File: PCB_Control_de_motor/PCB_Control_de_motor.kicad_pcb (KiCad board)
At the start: 2 copper layers, 100 x 50 mm, 0 parts

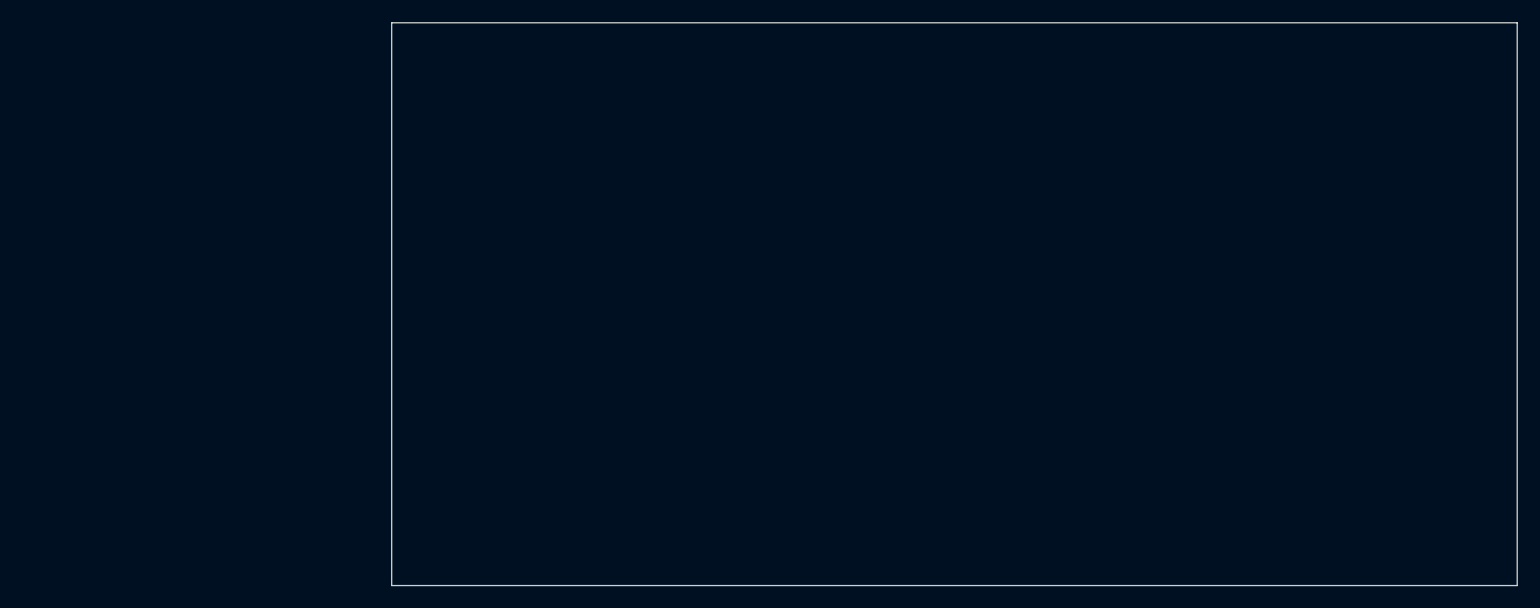
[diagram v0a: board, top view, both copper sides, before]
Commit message: Agregado de diodos TVS y avance del PCB con fuente y micro listo
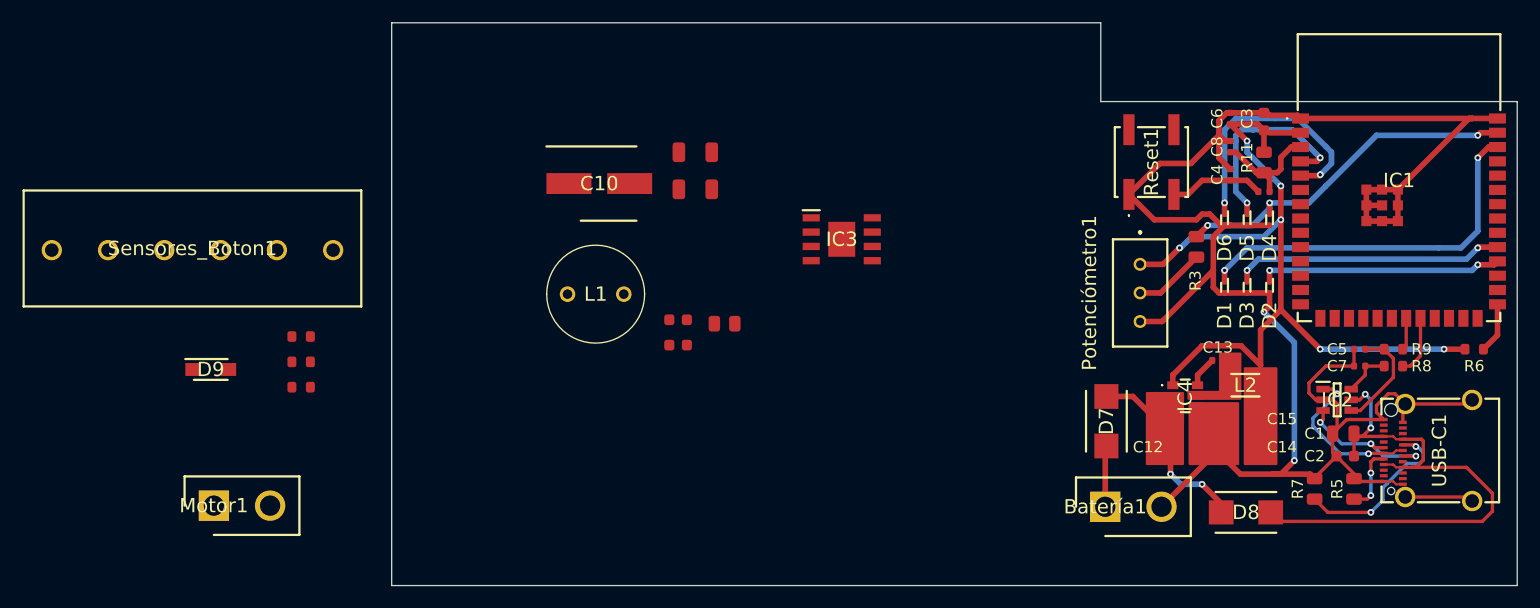
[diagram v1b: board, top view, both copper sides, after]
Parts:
- added Batería1: XT30UPB-M, SamacSys_Parts:SHDR2W160P0X500_1X2_1020X520X1070P, F.Cu at (153.4, 113.0)
- added C1: 22uF, PCM_JLCPCB:C_0805, F.Cu at (174.6, 106.5)
- added C10: 47uF, SamacSys_Parts:CAPAE660X820N, F.Cu at (108.4, 84.3)
- added C11: 100nF, PCM_JLCPCB:C_0603, F.Cu at (115.4, 98.6)
- added C12: 10uF, PCM_JLCPCB:C_0805, F.Cu at (160.7, 107.7)
- added C13: 100nF, PCM_JLCPCB:C_0402, F.Cu at (163.4, 100.0)
- added C14: 22uF, PCM_JLCPCB:C_0805, F.Cu at (165.6, 107.7)
- added C15: 22uF, PCM_JLCPCB:C_0805, F.Cu at (165.6, 105.2)
- added C2: 100nF, PCM_JLCPCB:C_0603, F.Cu at (174.7, 108.5)
- added C3: 22uF, PCM_JLCPCB:C_0603, F.Cu at (167.5, 78.8)
- added C4: 100nF, PCM_JLCPCB:C_0402, F.Cu at (164.5, 83.5)
- added C5: 1uF, PCM_JLCPCB:C_0402, F.Cu at (176.0, 99.0)
- added C6: 100nF, PCM_JLCPCB:C_0402, F.Cu at (164.5, 78.5)
- added C7: 1uF, PCM_JLCPCB:C_0402, F.Cu at (176.0, 100.5)
- added C8: 1uF, PCM_JLCPCB:C_0402, F.Cu at (164.5, 81.0)
- added C9: 100nF, PCM_JLCPCB:C_0603, F.Cu at (115.4, 96.4)
- added D1: ESD9B3.3ST5G, SamacSys_Parts:SODFL1006X40N, F.Cu at (164.0, 93.5)
- added D2: ESD9B3.3ST5G, SamacSys_Parts:SODFL1006X40N, F.Cu at (168.0, 93.5)
- added D3: ESD9B3.3ST5G, SamacSys_Parts:SODFL1006X40N, F.Cu at (166.0, 93.5)
- added D4: ESD9B3.3ST5G, SamacSys_Parts:SODFL1006X40N, F.Cu at (168.0, 87.5)
- added D5: ESD9B3.3ST5G, SamacSys_Parts:SODFL1006X40N, F.Cu at (166.0, 87.5)
- added D6: ESD9B3.3ST5G, SamacSys_Parts:SODFL1006X40N, F.Cu at (164.0, 87.5)
- added D7: SS210-E3_52T, SamacSys_Parts:DIONM5436X244N, F.Cu at (153.5, 105.4)
- added D8: SS210-E3_52T, SamacSys_Parts:DIONM5436X244N, F.Cu at (165.9, 113.5)
- added D9: SMF3.3, SamacSys_Parts:SOD3718X108N, F.Cu at (73.9, 100.8)
- added IC1: ESP32-S3-WROOM-1-N16, SamacSys_Parts:ESP32S3WROOM1N16, F.Cu at (179.5, 83.8)
- added IC2: USBLC6-2SC6, SamacSys_Parts:SOT95P280X145-6N, F.Cu at (174.0, 103.5)
- added IC3: DRV8871DDAR, SamacSys_Parts:SOIC127P600X170-9N, F.Cu at (130.0, 89.2)
- added IC4: AP63203WU-7, SamacSys_Parts:AP63203WU7, F.Cu at (160.5, 103.2)
- added L1: 100mH, SamacSys_Parts:RLB1014104KL, F.Cu at (105.6, 94.1)
- added L2: NLV25T-3R9J-PF, SamacSys_Parts:INDM2520X190N, F.Cu at (165.8, 102.2)
- added Motor1: XT30UPB-M, SamacSys_Parts:SHDR2W160P0X500_1X2_1020X520X1070P, F.Cu at (74.2, 112.9)
- added Potenciómetro1: 20k, SamacSys_Parts:3296W1503LF, F.Cu at (156.5, 91.5)
- added R1: 10kΩ, PCM_JLCPCB:R_0603, F.Cu at (82.0, 97.9)
- added R10: 0Ω, PCM_JLCPCB:R_0402, F.Cu at (167.5, 85.0)
- added R11: 10kΩ, PCM_JLCPCB:R_0805, F.Cu at (167.5, 82.4)
- added R12: 4.7kΩ, PCM_JLCPCB:R_1206, F.Cu at (117.0, 81.5)
- added R13: 4.7kΩ, PCM_JLCPCB:R_1206, F.Cu at (117.0, 84.8)
- added R14: 30kΩ, PCM_JLCPCB:R_0805, F.Cu at (119.6, 96.7)
- added R2: 10kΩ, PCM_JLCPCB:R_0603, F.Cu at (82.0, 100.1)
- added R3: 1kΩ, PCM_JLCPCB:R_0805, F.Cu at (161.5, 89.9)
- added R4: 10kΩ, PCM_JLCPCB:R_0603, F.Cu at (82.0, 102.4)
- added R5: 5.1kΩ, PCM_JLCPCB:R_0805, F.Cu at (175.5, 111.4)
- added R6: 4.7kΩ, PCM_JLCPCB:R_0603, F.Cu at (186.2, 99.0)
- added R7: 5.1kΩ, PCM_JLCPCB:R_0805, F.Cu at (172.0, 111.4)
- added R8: 33Ω, PCM_JLCPCB:R_0603, F.Cu at (179.0, 100.5)
- added R9: 33Ω, PCM_JLCPCB:R_0603, F.Cu at (179.0, 99.0)
- added Reset1: B3SL-1022P, SamacSys_Parts:B3SL1022P, F.Cu at (157.5, 82.4)
- added Sensores_Boton1: WJ128V-5.0-6P, SamacSys_Parts:WJ128V506P, F.Cu at (59.8, 90.2)
- added USB-C1: 12401832E402A, SamacSys_Parts:12401832E402A, F.Cu at (183.2, 108.0)
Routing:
- net GND: track 0.00 -> 181.5 mm, vias 0 -> 2
- net +3.3V: track 0.00 -> 75.5 mm, vias 0 -> 6
- net /5v_USB: track 0.00 -> 50.1 mm, vias 0 -> 2
- net /BOTON: track 0.00 -> 33.6 mm, vias 0 -> 2
- net /ADC: track 0.00 -> 31.9 mm, vias 0 -> 3
- net /LSC: track 0.00 -> 24.1 mm, vias 0 -> 2
- net /Driver/IN_2: track 0.00 -> 22.9 mm, vias 0 -> 2
- net /LSA: track 0.00 -> 21.6 mm, vias 0 -> 2
- net Net-(D7-K): track 0.00 -> 19.6 mm, vias 0 -> 2
- net /Driver/IN_1: track 0.00 -> 18.0 mm, vias 0 -> 2
- net Net-(USB-C1-CC2): track 0.00 -> 15.5 mm, vias 0 -> 2
- net Net-(IC2-I/O1_1): track 0.00 -> 14.4 mm, vias 0 -> 2
- net Net-(IC2-I/O2_1): track 0.00 -> 13.3 mm, vias 0 -> 3
- net EN_ESP32: track 0.00 -> 10.4 mm
- net Net-(IC2-I/O2_2): track 0.00 -> 9.49 mm
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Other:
- outline, holes or cut-outs redrawn

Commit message: PCB casi terminado
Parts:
- moved D9 95.7 mm to (169.6, 102.1), turned to -90 degrees
- moved Sensores_Boton1 90.0 mm to (148.8, 76.8), turned to 180 degrees
- moved R4 68.2 mm to (149.8, 95.8), turned to 90 degrees
- moved R1 68.0 mm to (149.8, 92.7), turned to 90 degrees
- moved R2 67.9 mm to (149.8, 99.0), turned to 90 degrees
- moved Motor1 50.7 mm to (123.2, 99.8), turned to -90 degrees
- moved L1 34.5 mm to (137.1, 108.3), turned to -90 degrees
- moved C11 30.0 mm to (143.0, 110.5), turned to 90 degrees
- moved R12 29.3 mm to (145.1, 89.7), turned to 90 degrees
- moved R13 25.5 mm to (142.0, 89.7), turned to 90 degrees
- moved C10 25.1 mm to (132.7, 90.7), turned to 180 degrees
- moved C9 22.4 mm to (137.8, 96.9)
- moved R14 21.6 mm to (141.2, 96.9), turned to 180 degrees
- moved IC3 15.2 mm to (139.6, 101.0), turned to 180 degrees
- moved C12 1.20 mm to (159.5, 108.0)
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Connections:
- C10 pad 2: GND -> Net-(C10--)
- C11 pad 2: Net-(IC3-PGND) -> Net-(C10--)
- IC3 pad 7: Net-(IC3-PGND) -> Net-(C10--)
- L1 pad 1: Net-(IC3-PGND) -> Net-(C10--)
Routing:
- net GND: track 181.5 -> 296.5 mm, vias 2 -> 4
- net /LSA: track 21.6 -> 100.9 mm, vias 2 -> 3
- net /LSC: track 24.1 -> 80.9 mm, vias 2 -> 3
- net /Driver/IN_2: track 22.9 -> 61.7 mm, vias 2 -> 4
- net /BOTON: track 33.6 -> 69.5 mm, vias 2 -> 3
- net /Driver/IN_1: track 18.0 -> 52.6 mm, vias 2 -> 4
- net +3.3V: track 75.5 -> 109.4 mm, vias 6 -> 10
- net Net-(C10--): track 0.00 -> 32.9 mm, vias 0 -> 3
- net +12V: track 5.44 -> 38.3 mm
- net Net-(D7-K): track 19.6 -> 24.4 mm
- net Net-(IC3-ILIM): track 0.00 -> 2.23 mm

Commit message: PCB listo
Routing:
- net Net-(C10--): vias 3 -> 22
- net GND: vias 4 -> 50
- added copper zone on B.Cu, net GND
- added copper zone on F.Cu, net GND
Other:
- board size 100 x 50 mm -> 71 x 47.5 mm

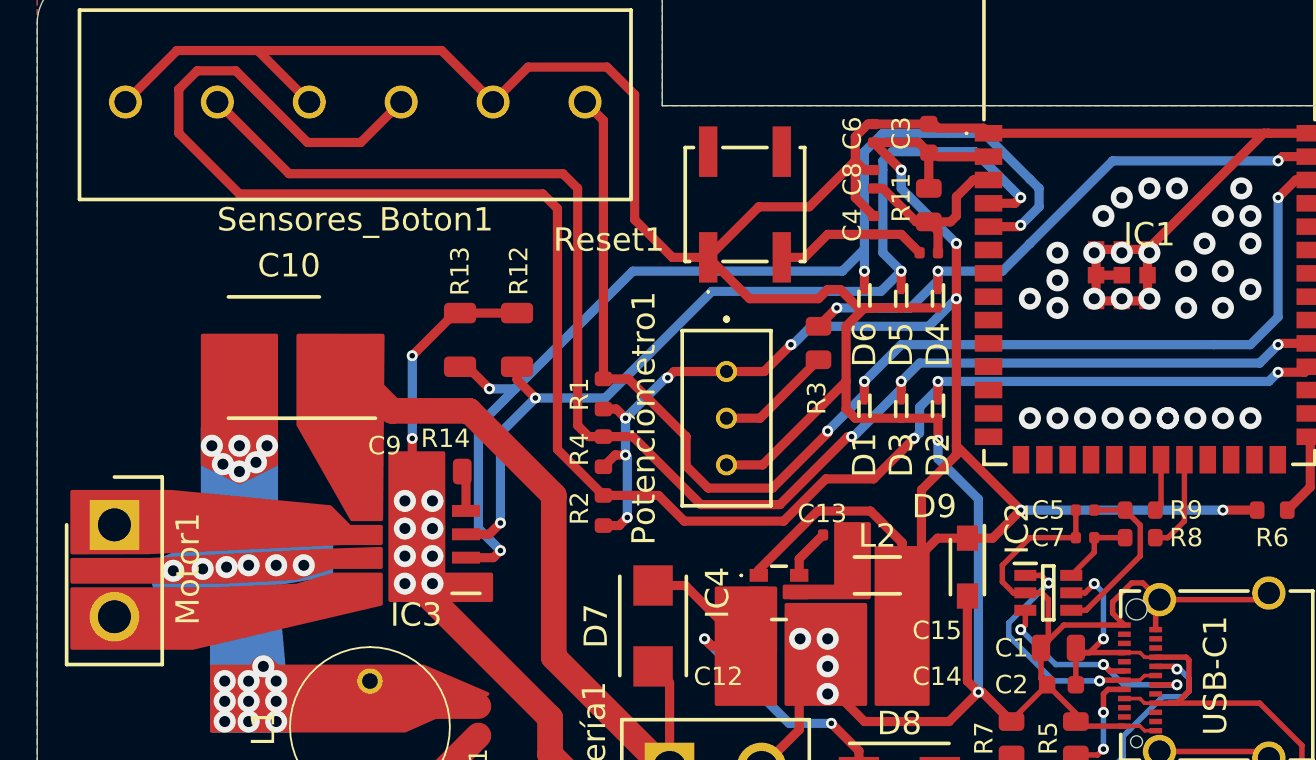
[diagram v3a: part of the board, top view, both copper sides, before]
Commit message: Correción del PCB, archivos de fabricación y BOM
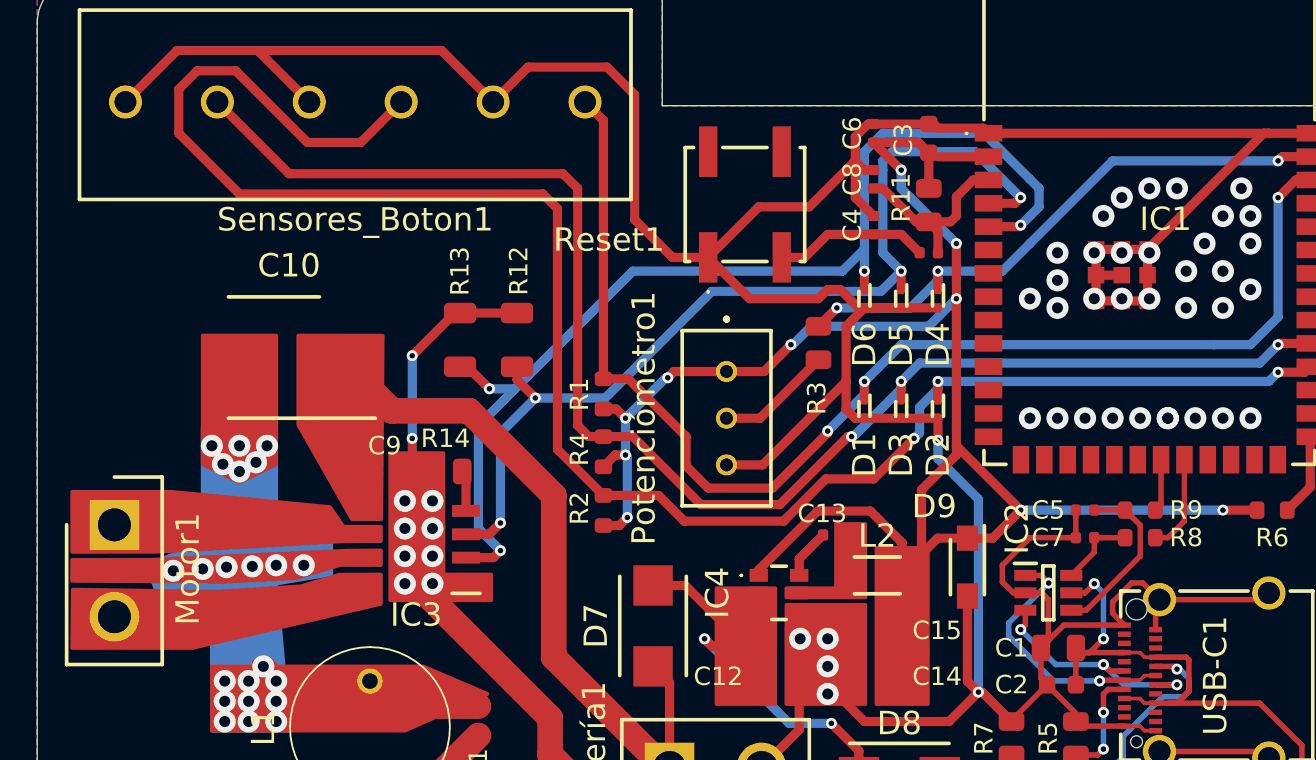
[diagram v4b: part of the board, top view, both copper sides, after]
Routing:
- net +3.3V: track 109.4 -> 108.3 mm
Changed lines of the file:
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@@
 	)
 	(setup
+		(stackup
+			(layer "F.SilkS"
+				(type "Top Silk Screen")
+			)
+			(layer "F.Paste"
+				(type "Top Solder Paste")
+			)
+			(layer "F.Mask"
+				(type "Top Solder Mask")
+				(thickness 0.01)
+			)
+			(layer "F.Cu"
+				(type "copper")
+				(thickness 0.035)
+			)
+			(layer "dielectric 1"
+				(type "core")
+				(thickness 1.51)
+				(material "FR4")
+				(epsilon_r 4.5)
+				(loss_tangent 0.02)
+			)
+			(layer "B.Cu"
+				(type "copper")
+				(thickness 0.035)
+			)
+			(layer "B.Mask"
+				(type "Bottom Solder Mask")
+				(thickness 0.01)
+			)
+			(layer "B.Paste"
+				(type "Bottom Solder Paste")
+			)
+			(layer "B.SilkS"
+				(type "Bottom Silk Screen")
+			)
+			(copper_finish "None")
+			(dielectric_constraints no)
+		)
 		(pad_to_mask_clearance 0)
 		(allow_soldermask_bridges_in_footprints no)
@@
 			(outputformat 1)
 			(mirror no)
-			(drillshape 1)
+			(drillshape 0)
 			(scaleselection 1)
-			(outputdirectory "")
+			(outputdirectory "Archivos_de_fabricacion/")
 		)
 	)
@@
 		(tags "Integrated Circuit")
 		(property "Reference" "IC1"
-			(at 0 0.25 0)
+			(at 0.88 -0.59 0)
 			(layer "F.SilkS")
 			(effects
@@
 		)
 		(fp_text user "${REFERENCE}"
-			(at 0 0.25 0)
+			(at 0.89 -0.58 0)
 			(layer "F.Fab")
 			(effects
@@
 		(tags "capacitor")
 		(property "Reference" "C3"
-			(at 0.28 -1.5 90)
+			(at -0.08 -1.38 90)
 			(layer "F.SilkS")
 			(effects
@@
 	(gr_poly
 		(pts
-			(xy 162.45 99.75) (xy 164.25 99.75) (xy 164.25 103.75) (xy 159.65 103.75) (xy 159.65 103.15) (xy 162.45 103.15)
+			(xy 162.45 99.75) (xy 164.05 99.75) (xy 164.05 103.75) (xy 159.75 103.75) (xy 159.75 103.25) (xy 162.45 103.25)
 		)
 		(stroke
@@
 	(gr_poly
 		(pts
-			(xy 137.7 101.1) (xy 134.7 101.2) (xy 125.158007 101.7) (xy 120.9 101.7) (xy 120.9 102.9) (xy 129.2 102.9)
-			(xy 133.1 102.7) (xy 135.1 102.1) (xy 137.7 102.1)
+			(xy 137.7 101.189281) (xy 135.92 101.2) (xy 125.158007 101.7) (xy 120.9 101.7) (xy 120.89 102.85)
+			(xy 129.2 102.9) (xy 133.1 102.7) (xy 135.466667 101.99) (xy 137.7 101.99)
 		)
 		(stroke
@@
 	(gr_poly
 		(pts
-			(xy 120.9 106.5) (xy 127.453844 106.5) (xy 137.7 104.1) (xy 137.7 102.5) (xy 135.149999 102.5) (xy 133.1 103.1)
-			(xy 128.50044 103.3) (xy 120.9 103.3)
+			(xy 120.9 106.5) (xy 127.453844 106.5) (xy 137.7 104.1) (xy 137.7 102.5) (xy 135.43 102.51) (xy 133.34 103.14)
+			(xy 128.73 103.44) (xy 120.93 103.32)
 		)
 		(stroke
@@
 	(gr_poly
 		(pts
-			(xy 120.9 98) (xy 126.3 98) (xy 134.932001 98.832001) (xy 136 99.9) (xy 137.7 99.9) (xy 137.7 100.8)
-			(xy 135.6 100.8) (xy 125 101.3) (xy 120.9 101.308614)
+			(xy 120.9 98) (xy 126.3 98) (xy 134.932001 98.832001) (xy 135.66 99.9) (xy 137.7 99.9) (xy 137.7 100.69)
+			(xy 135.61 100.7) (xy 125.564449 101.267963) (xy 120.9 101.277763)
 		)
 		(stroke
@@
 	)
 	(segment
-		(start 165.45 104.55)
-		(end 166.2 105.3)
-		(width 0.5)
-		(layer "F.Cu")
-		(net 3)
-	)
-	(segment
 		(start 170.975 100.525)
 		(end 172.5 99)
@@
 	)
 	(via
-		(at 130.5 102)
+		(at 132 109.4)
 		(size 1.2)
 		(drill 0.6)
@@
 	)
 	(via
-		(at 132 109.4)
+		(at 130 95.5)
 		(size 1.2)
 		(drill 0.6)
@@
 	)
 	(via
-		(at 130 95.5)
+		(at 130.7 102.06)
 		(size 1.2)
 		(drill 0.6)

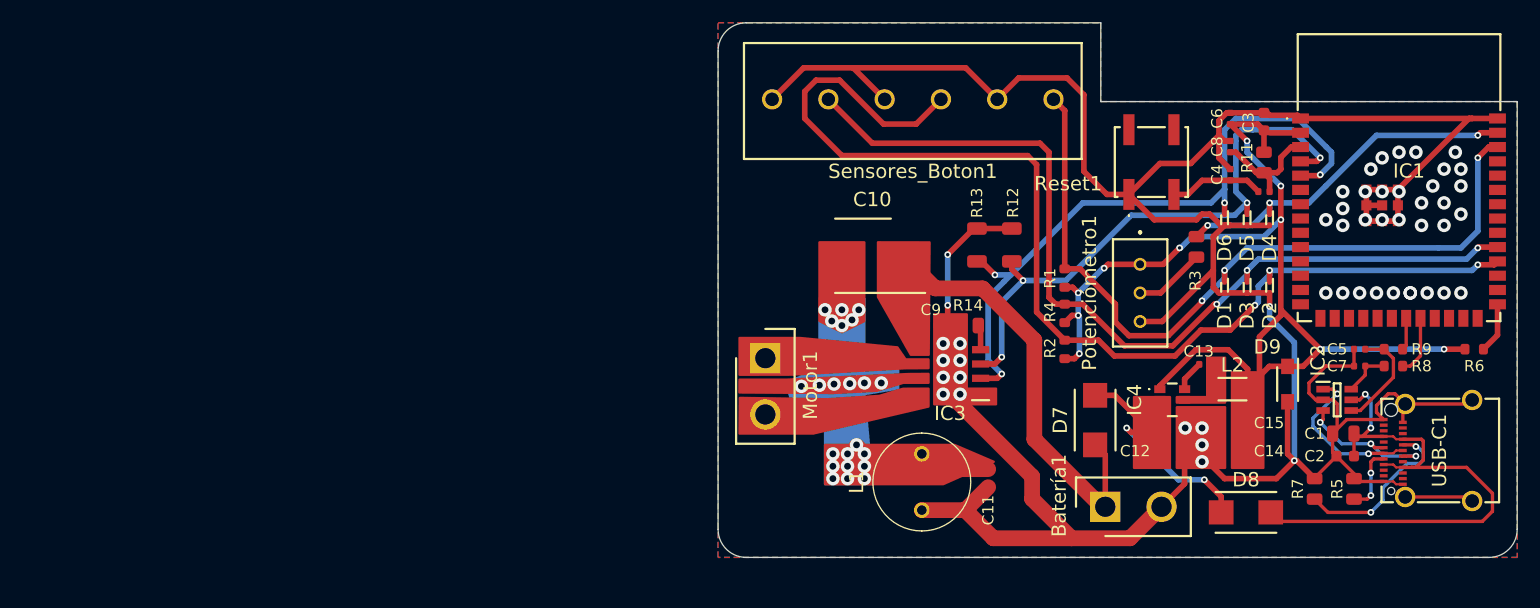
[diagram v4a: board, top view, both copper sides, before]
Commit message: Cambio del capacitor y rediseño de las pistas del driver con sus componentes
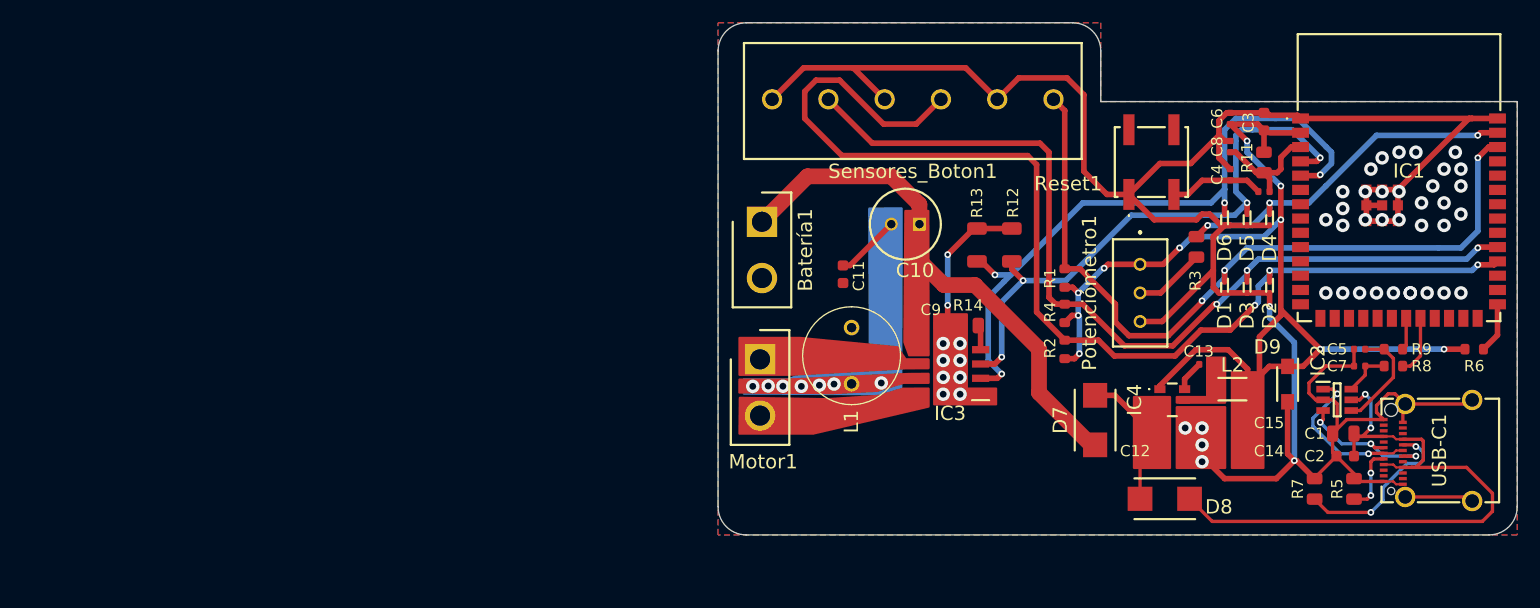
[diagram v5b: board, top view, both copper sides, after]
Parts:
- C10: value 47uF -> EEUFC1H470; footprint SamacSys_Parts:CAPAE660X820N -> SamacSys_Parts:CAPPRD250W55D630H1220
- moved Batería1 39.6 mm to (122.9, 87.7), turned to -90 degrees
- moved C11 22.3 mm to (130.1, 92.3)
- moved L1 8.81 mm to (130.9, 102.1), turned to 90 degrees
- moved D8 7.31 mm to (158.7, 112.3)
- moved C10 5.05 mm to (136.9, 87.9)
- moved Motor1 0.48 mm to (122.7, 99.9)
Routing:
- net GND: track 296.5 -> 247.1 mm
- net +12V: track 38.3 -> 55.4 mm
- net Net-(C10--): track 32.9 -> 21.4 mm, vias 22 -> 7
- net Net-(D7-K): track 24.4 -> 16.0 mm, vias 2 -> 0
- net /5v_USB: track 50.1 -> 57.8 mm
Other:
- board size 71 x 47.5 mm -> 71 x 45.5 mm
